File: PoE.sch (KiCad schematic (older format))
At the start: 25 parts, among them IC1 TPS2378DDA

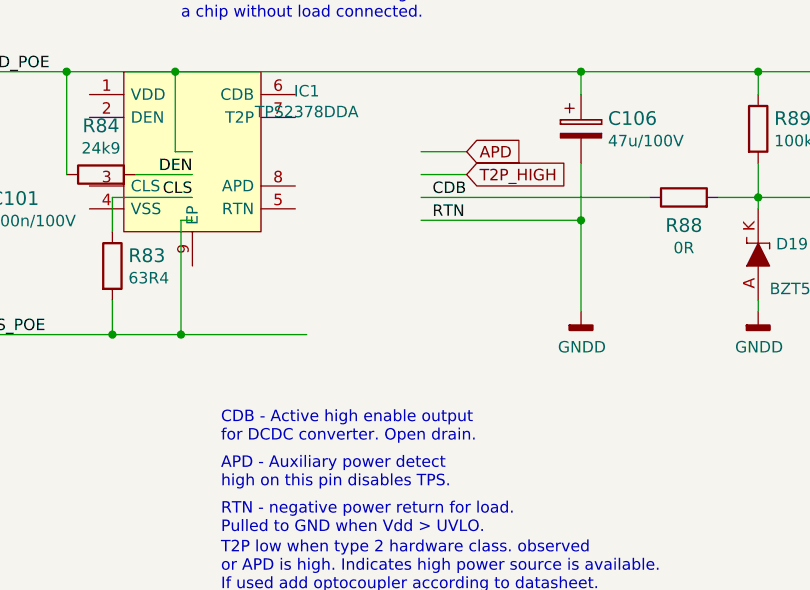
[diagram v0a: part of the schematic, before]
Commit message: Change comment on CDB
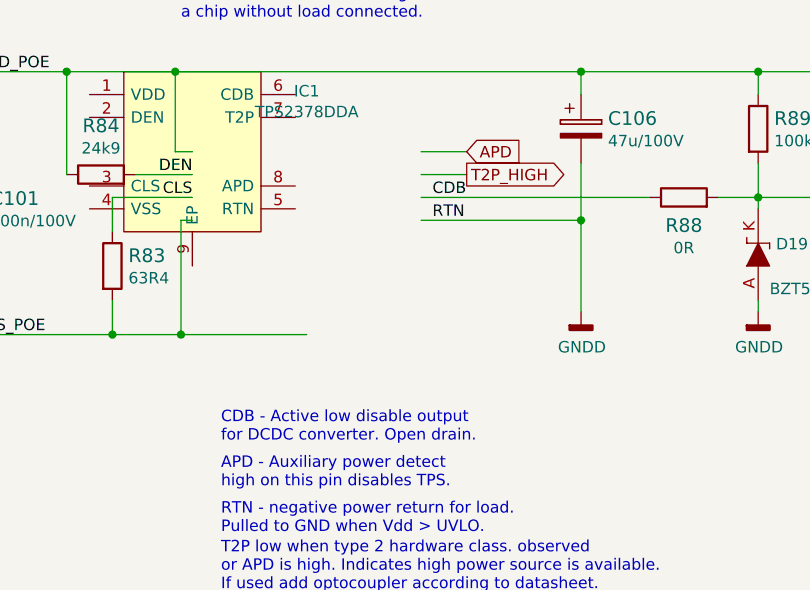
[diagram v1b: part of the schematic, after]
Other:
- note added: "CDB - Active low disable output \nfor DCDC converter. Open drain."
- note removed: "CDB - Active high enable output \nfor DCDC converter. Open drain."
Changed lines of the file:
@@
 $EndComp
 Text Notes 5975 6250 0    50   ~ 0
-CDB - Active high enable output \nfor DCDC converter. Open drain.
+CDB - Active low disable output \nfor DCDC converter. Open drain.
 Wire Wire Line
 	8325 5625 8325 5675
@@
 	1    0    0    -1
 $EndComp
-Text GLabel 7050 5075 2    50   Input ~ 0
+Text GLabel 7050 5075 2    50   Output ~ 0
 T2P_HIGH
 Wire Wire Line

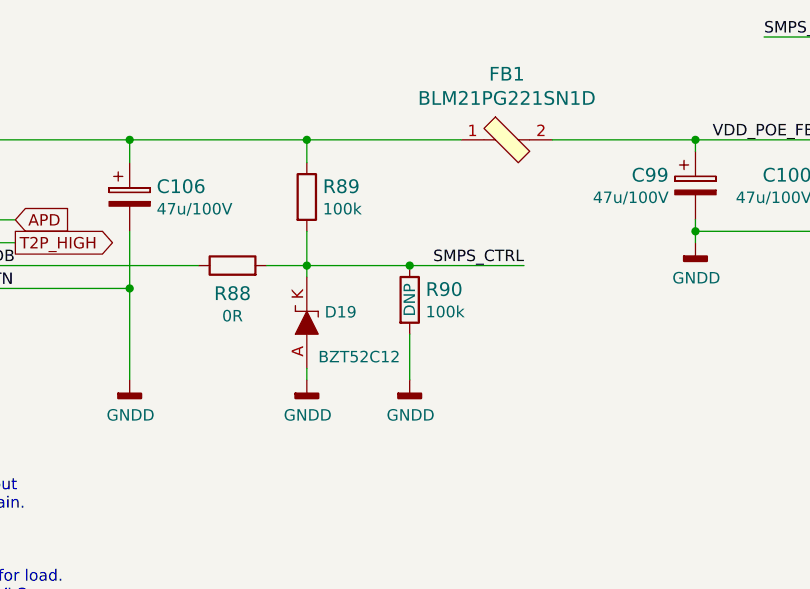
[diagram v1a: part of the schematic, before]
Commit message: Remove zener diode, annotate parts
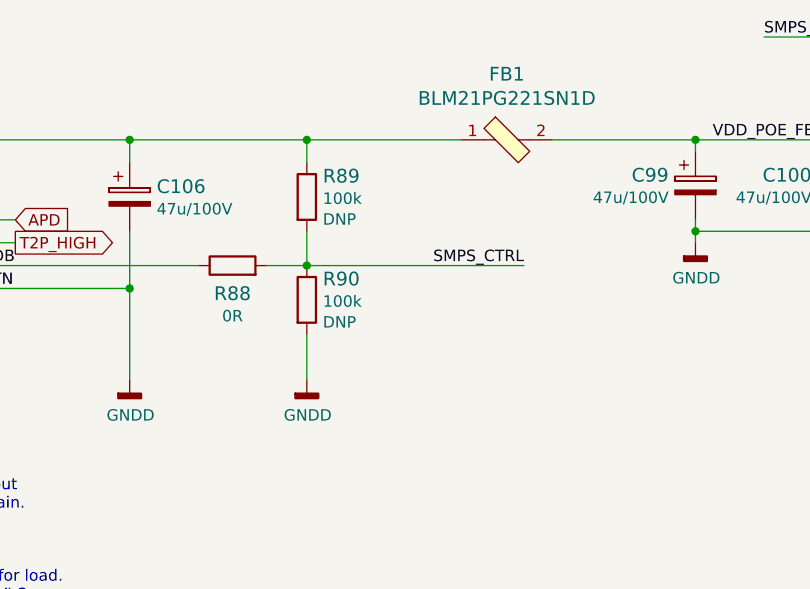
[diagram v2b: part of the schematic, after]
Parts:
- removed D19: BZT52C12, sa800u-baseboard-hw-footprints:SOD-123, symbol sa800u-baseboard-hw:BZT52C12
- R89: DNP (none) -> DNP
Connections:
- wire segments 95 -> 92
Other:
- moved on the sheet: R90
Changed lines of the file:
@@
 Wire Wire Line
 	10875 4825 10775 4825
-Wire Wire Line
-	8775 5175 9275 5175
 Text Label 9275 5175 2    50   ~ 0
 SMPS_CTRL
-Connection ~ 8775 5175
 Wire Wire Line
 	10650 5025 10650 4975
@@
 $EndComp
 Wire Wire Line
-	8775 5475 8775 5675
+	8325 5475 8325 5675
 $Comp
 L sa800u-baseboard-hw:GNDD #PWR0155
 U 1 1 61A460FF
-P 8775 5675
-F 0 "#PWR0155" H 8775 5425 50  0001 C CNN
-F 1 "GNDD" H 8779 5520 50  0000 C CNN
-F 2 "" H 8775 5675 50  0001 C CNN
-F 3 "" H 8775 5675 50  0001 C CNN
-	1    8775 5675
+P 8325 5675
+F 0 "#PWR0155" H 8325 5425 50  0001 C CNN
+F 1 "GNDD" H 8329 5520 50  0000 C CNN
+F 2 "" H 8325 5675 50  0001 C CNN
+F 3 "" H 8325 5675 50  0001 C CNN
+	1    8325 5675
 	1    0    0    -1
 $EndComp
@@
 L sa800u-baseboard-hw:R_100k_0402 R90
 U 1 1 61A46108
-P 8775 5325
-F 0 "R90" V 8730 5395 60  0000 L CNN
-F 1 "R_100k_0402" H 8775 5175 60  0001 C CNN
-F 2 "sa800u-baseboard-hw-footprints:0402-res" H 8975 5525 60  0001 L CNN
-F 3 "" H 8775 5325 50  0001 C CNN
-F 4 "VISHAY" H 8975 5725 60  0001 L CNN "Manufacturer"
-F 5 "CRCW0402100KFKEDHP" H 8975 5625 60  0001 L CNN "MPN"
-F 6 "100k" V 8828 5395 50  0000 L CNN "Val"
-F 7 "DNP" H 8775 5325 50  0000 C CNN "DNP"
-	1    8775 5325
+P 8325 5325
+F 0 "R90" V 8234 5395 60  0000 L CNN
+F 1 "R_100k_0402" H 8325 5175 60  0001 C CNN
+F 2 "sa800u-baseboard-hw-footprints:0402-res" H 8525 5525 60  0001 L CNN
+F 3 "" H 8325 5325 50  0001 C CNN
+F 4 "VISHAY" H 8525 5725 60  0001 L CNN "Manufacturer"
+F 5 "CRCW0402100KFKEDHP" H 8525 5625 60  0001 L CNN "MPN"
+F 6 "100k" V 8332 5395 50  0000 L CNN "Val"
+F 7 "DNP" V 8423 5395 50  0000 L CNN "DNP"
+	1    8325 5325
 	0    1    1    0
 $EndComp
@@
 	1    0    0    -1
 $EndComp
-$Comp
-L sa800u-baseboard-hw:GNDD #PWR0154
-U 1 1 61A46123
-P 8325 5675
-F 0 "#PWR0154" H 8325 5425 50  0001 C CNN
-F 1 "GNDD" H 8329 5520 50  0000 C CNN
-F 2 "" H 8325 5675 50  0001 C CNN
-F 3 "" H 8325 5675 50  0001 C CNN
-	1    8325 5675
-	1    0    0    -1
-$EndComp
 Wire Wire Line
 	8325 5025 8325 5175
@@
 U 1 1 61A46133
 P 8325 4875
-F 0 "R89" V 8280 4945 60  0000 L CNN
+F 0 "R89" V 8234 4945 60  0000 L CNN
 F 1 "R_100k_0402" H 8325 4725 60  0001 C CNN
 F 2 "sa800u-baseboard-hw-footprints:0402-res" H 8525 5075 60  0001 L CNN
@@
 F 4 "VISHAY" H 8525 5275 60  0001 L CNN "Manufacturer"
 F 5 "CRCW0402100KFKEDHP" H 8525 5175 60  0001 L CNN "MPN"
-F 6 "100k" V 8378 4945 50  0000 L CNN "Val"
+F 6 "100k" V 8332 4945 50  0000 L CNN "Val"
+F 7 "DNP" V 8423 4945 50  0000 L CNN "DNP"
 	1    8325 4875
 	0    1    1    0
 $EndComp
-Wire Wire Line
-	8325 5175 8775 5175
 Connection ~ 8325 5175
 Wire Wire Line
@@
 	1    0    0    -1
 $EndComp
-$Comp
-L sa800u-baseboard-hw:BZT52C12 D19
-U 1 1 6286AAC9
-P 8325 5425
-F 0 "D19" V 8371 5347 50  0000 R CNN
-F 1 "BZT52C12" V 8175 5375 50  0000 R CNN
-F 2 "sa800u-baseboard-hw-footprints:SOD-123" H 8325 5425 50  0001 C CNN
-F 3 "https://www.farnell.com/datasheets/1670962.pdf" H 8325 5425 50  0001 C CNN
-F 4 "BZT52C12" H 8325 5425 50  0001 C CNN "MPN"
-F 5 "DIODES INC." H 8325 5425 50  0001 C CNN "Manufacturer"
-	1    8325 5425
-	0    -1   -1   0
-$EndComp
 Text Notes 5975 6250 0    50   ~ 0
 CDB - Active low disable output \nfor DCDC converter. Open drain.
-Wire Wire Line
-	8325 5625 8325 5675
-Wire Wire Line
-	8325 5225 8325 5175
 $Comp
 L sa800u-baseboard-hw:GNDD #PWR0152
@@
 Text Notes 11000 3600 0    79   ~ 16
 5V regulator
+Wire Wire Line
+	8325 5175 9275 5175
 $EndSCHEMATC

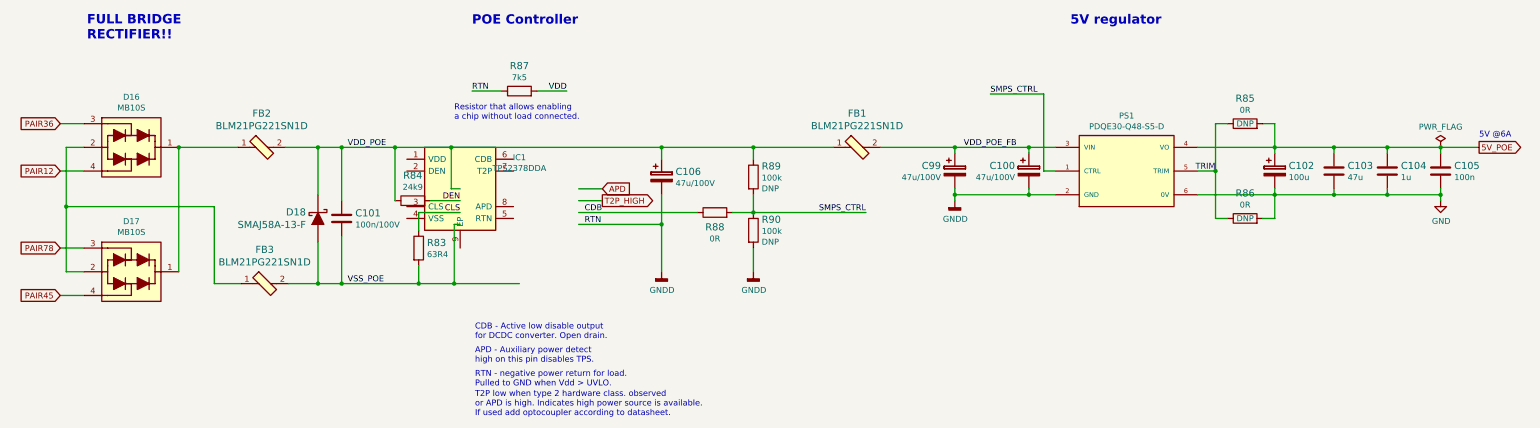
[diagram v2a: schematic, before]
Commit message: Remove ferrite bead and 47uF capacitor
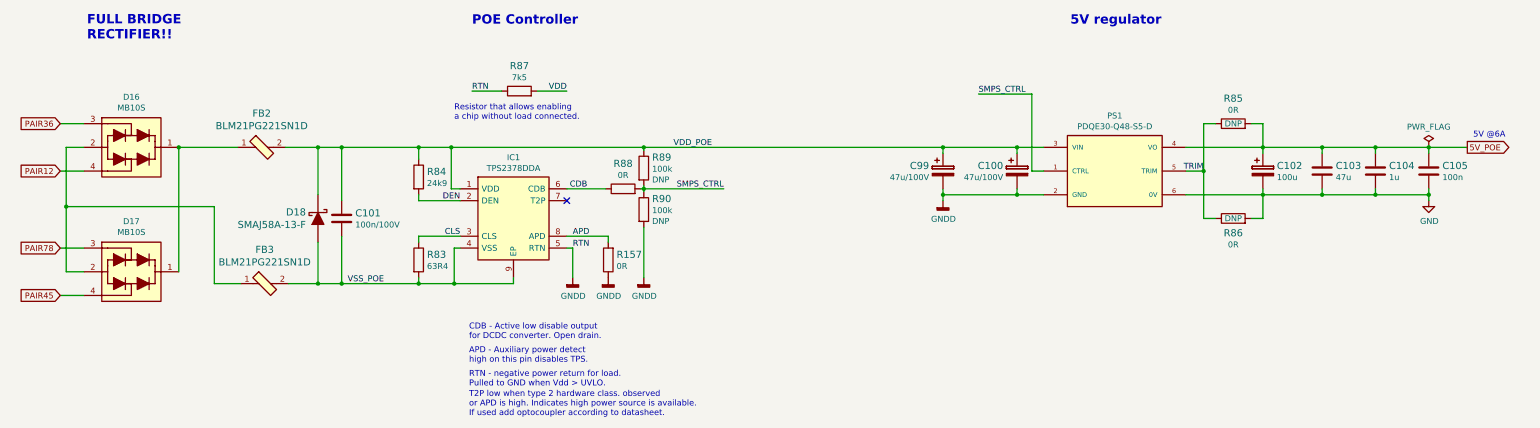
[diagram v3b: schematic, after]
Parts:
- removed C106: C_47u_ELEC_100V, sa800u-baseboard-hw-footprints:CP_Elec_10x10.5, symbol sa800u-baseboard-hw:C_47u_ELEC_100V
- removed FB1: BLM21PG221SN1D, sa800u-baseboard-hw-footprints:0805-res, symbol sa800u-baseboard-hw:BLM21PG221SN1D
- added R157: R_0R_0402, sa800u-baseboard-hw-footprints:0402-res, symbol sa800u-baseboard-hw:R_0R_0402
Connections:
- net labels removed: T2P_HIGH, VDD_POE_FB
- wire segments 92 -> 91
- no-connect marks 0 -> 1
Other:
- moved on the sheet: C100, C102, C103, C104, C105, C99, IC1, PS1, R83, R84, R85, R86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

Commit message: Add additional load to VDD_POE
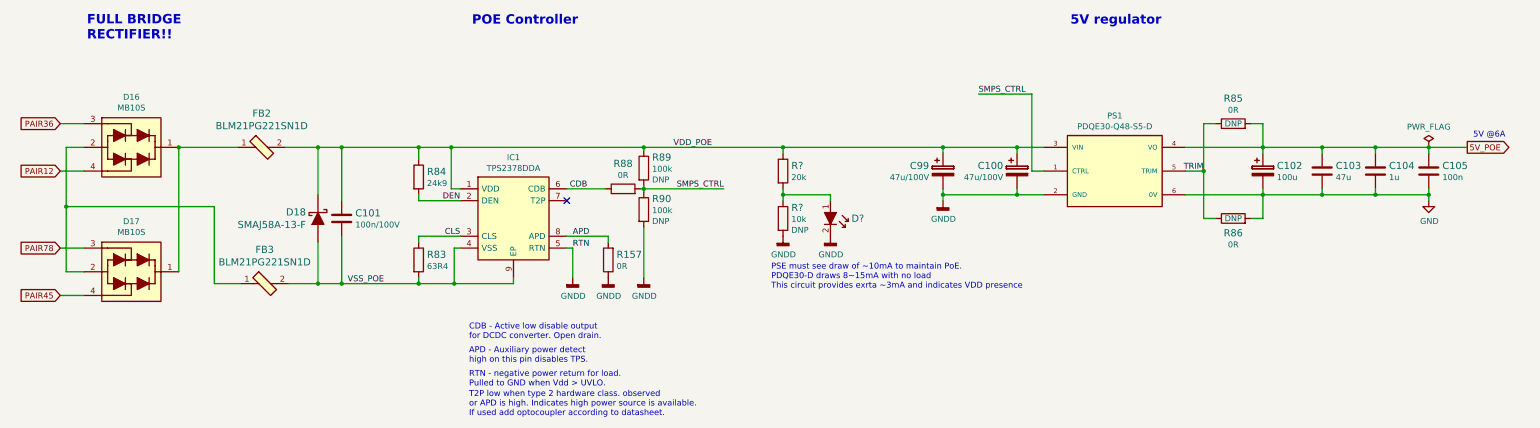
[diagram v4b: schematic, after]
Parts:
- removed R87: R_7k5_0402, sa800u-baseboard-hw-footprints:0402-res, symbol sa800u-baseboard-hw:R_7k5_0402
- added D?: KP-1608EC, sa800u-baseboard-hw-footprints:LED_0603, symbol sa800u-baseboard-hw:KP-1608EC
- added R?: R_20k_0603, sa800u-baseboard-hw-footprints:0603-res, symbol sa800u-baseboard-hw:R_20k_0603
- added R?: R_10k_0603, sa800u-baseboard-hw-footprints:0603-res, symbol sa800u-baseboard-hw:R_10k_0603
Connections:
- net GNDD: now also D?.2, R?.2
- net VDD_POE: now also R?.1
- new net: D?.1, R?.1, R?.2
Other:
- note added: "PSE must see draw of ~~10mA to maintain PoE.\nPDQE30-D draws 8~~15mA with no load\nThis circuit provides exrta ~~3mA and indicates VDD presence"
- note removed: "Resistor that allows enabling\na chip without load connected."
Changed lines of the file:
@@
 	14025 5025 14025 5075
 Wire Wire Line
-	11975 5025 12625 5025
-Wire Wire Line
 	12125 4825 11975 4825
-Text Label 10225 4175 0    50   ~ 0
-SMPS_CTRL
-Wire Wire Line
-	10675 4825 10675 4175
 Wire Wire Line
 	10775 4825 10675 4825
 Text Label 8075 4975 2    50   ~ 0
 SMPS_CTRL
-Wire Wire Line
-	10550 5025 10550 4975
-Wire Wire Line
-	10775 5025 10550 5025
 $Comp
 L sa800u-baseboard-hw:PDQE30-Q48-S5-D PS1
@@
 F 6 "CUI" H 11375 4825 50  0001 L BNN "Manufacturer"
 	1    11375 4825
-	1    0    0    -1
-$EndComp
-$Comp
-L sa800u-baseboard-hw:GNDD #PWR0150
-U 1 1 61A460D6
-P 9925 5075
-F 0 "#PWR0150" H 9925 4825 50  0001 C CNN
-F 1 "GNDD" H 9929 4920 50  0000 C CNN
-F 2 "" H 9925 5075 50  0001 C CNN
-F 3 "" H 9925 5075 50  0001 C CNN
-	1    9925 5075
-	1    0    0    -1
-$EndComp
-$Comp
-L sa800u-baseboard-hw:C_47u_ELEC_100V C100
-U 1 1 61A460E0
-P 10550 4775
-F 0 "C100" H 10433 4770 60  0000 R CNN
-F 1 "C_47u_ELEC_100V" H 10550 4625 60  0001 C CNN
-F 2 "sa800u-baseboard-hw-footprints:CP_Elec_10x10.5" H 10750 4975 60  0001 L CNN
-F 3 "https://industrial.panasonic.com/cdbs/www-data/pdf/RDE0000/ABA0000C1151.pdf" H 10550 4775 50  0001 C CNN
-F 4 "PANASONIC" H 10750 5175 60  0001 L CNN "Manufacturer"
-F 5 "EEEHA2A470UP" H 10750 5075 60  0001 L CNN "MPN"
-F 6 "47u/100V" H 10433 4672 50  0000 R CNN "Val"
-	1    10550 4775
-	1    0    0    -1
-$EndComp
-$Comp
-L sa800u-baseboard-hw:C_47u_ELEC_100V C99
-U 1 1 61A460EB
-P 9925 4775
-F 0 "C99" H 9808 4770 60  0000 R CNN
-F 1 "C_47u_ELEC_100V" H 9925 4625 60  0001 C CNN
-F 2 "sa800u-baseboard-hw-footprints:CP_Elec_10x10.5" H 10125 4975 60  0001 L CNN
-F 3 "https://industrial.panasonic.com/cdbs/www-data/pdf/RDE0000/ABA0000C1151.pdf" H 9925 4775 50  0001 C CNN
-F 4 "PANASONIC" H 10125 5175 60  0001 L CNN "Manufacturer"
-F 5 "EEEHA2A470UP" H 10125 5075 60  0001 L CNN "MPN"
-F 6 "47u/100V" H 9808 4672 50  0000 R CNN "Val"
-	1    9925 4775
 	1    0    0    -1
 $EndComp
@@
 Text Notes 5925 6900 0    50   ~ 0
 T2P low when type 2 hardware class. observed\nor APD is high. Indicates high power source is available. \nIf used add optocoupler according to datasheet.
-Text Notes 5800 4400 0    50   ~ 0
-Resistor that allows enabling\na chip without load connected.
 Text Label 6800 5475 0    50   ~ 0
 RTN
@@
 Connection ~ 13575 5025
 Connection ~ 13125 5025
-Wire Wire Line
-	10550 4625 10550 4675
-Wire Wire Line
-	9925 4975 9925 5025
-Wire Wire Line
-	9925 4625 9925 4675
 Connection ~ 10550 4625
 Wire Wire Line
 	10550 4625 10775 4625
-Connection ~ 10550 5025
-Connection ~ 9925 4625
 Wire Wire Line
 	9925 4625 10550 4625
-Connection ~ 9925 5025
-Wire Wire Line
-	9925 5025 10550 5025
-Wire Wire Line
-	9925 5075 9925 5025
 Connection ~ 4650 4625
 Connection ~ 4650 5775
@@
 Text Label 6775 4975 0    50   ~ 0
 CDB
-Text Label 5950 4150 0    50   ~ 0
-RTN
-Wire Wire Line
-	6200 4150 5950 4150
-Wire Wire Line
-	6750 4150 6500 4150
-Text Label 6750 4150 2    50   ~ 0
-VDD
 $Comp
 L sa800u-baseboard-hw:TPS2378DDA IC1
@@
 Text Label 7650 4625 0    50   ~ 0
 VDD_POE
-$Comp
-L sa800u-baseboard-hw:R_7k5_0402 R87
-U 1 1 66578F6C
-P 6350 4150
-F 0 "R87" H 6350 4363 60  0000 C CNN
-F 1 "R_7k5_0402" H 6350 4000 60  0001 C CNN
-F 2 "sa800u-baseboard-hw-footprints:0402-res" H 6550 4350 60  0001 L CNN
-F 3 "" H 6350 4150 50  0001 C CNN
-F 4 "YAGEO" H 6550 4550 60  0001 L CNN "Manufacturer"
-F 5 "RC0402FR-077K5L" H 6550 4450 60  0001 L CNN "MPN"
-F 6 "7k5" H 6350 4265 50  0000 C CNN "Val"
-	1    6350 4150
-	1    0    0    -1
-$EndComp
 Text Label 5850 5075 2    50   ~ 0
 DEN
@@
 	12525 4425 12625 4425
 Wire Wire Line
-	10225 4175 10675 4175
-Wire Wire Line
 	12125 4425 12225 4425
 Wire Wire Line
@@
 Wire Wire Line
 	7400 4650 7400 4625
-Connection ~ 7400 4625
 Wire Wire Line
 	5775 4625 7400 4625
@@
 Text GLabel 2475 5475 0    50   Input ~ 0
 PAIR78
-Wire Wire Line
-	7400 4625 9925 4625
+Connection ~ 9925 4625
+Connection ~ 7400 4625
+Wire Wire Line
+	7400 4625 8575 4625
+$Comp
+L sa800u-baseboard-hw:GNDD #PWR0150
+U 1 1 61A460D6
+P 9925 5075
+F 0 "#PWR0150" H 9925 4825 50  0001 C CNN
+F 1 "GNDD" H 9929 4920 50  0000 C CNN
+F 2 "" H 9925 5075 50  0001 C CNN
+F 3 "" H 9925 5075 50  0001 C CNN
+	1    9925 5075
+	1    0    0    -1
+$EndComp
+Wire Wire Line
+	9925 5075 9925 5025
+Connection ~ 9925 5025
+Wire Wire Line
+	9925 5025 10550 5025
+Wire Wire Line
+	10550 5025 10550 4975
+Wire Wire Line
+	10550 4625 10550 4675
+$Comp
+L sa800u-baseboard-hw:C_47u_ELEC_100V C100
+U 1 1 61A460E0
+P 10550 4775
+F 0 "C100" H 10433 4770 60  0000 R CNN
+F 1 "C_47u_ELEC_100V" H 10550 4625 60  0001 C CNN
+F 2 "sa800u-baseboard-hw-footprints:CP_Elec_10x10.5" H 10750 4975 60  0001 L CNN
+F 3 "https://industrial.panasonic.com/cdbs/www-data/pdf/RDE0000/ABA0000C1151.pdf" H 10550 4775 50  0001 C CNN
+F 4 "PANASONIC" H 10750 5175 60  0001 L CNN "Manufacturer"
+F 5 "EEEHA2A470UP" H 10750 5075 60  0001 L CNN "MPN"
+F 6 "47u/100V" H 10433 4672 50  0000 R CNN "Val"
+	1    10550 4775
+	1    0    0    -1
+$EndComp
+Wire Wire Line
+	9925 4975 9925 5025
+Wire Wire Line
+	9925 4625 9925 4675
+$Comp
+L sa800u-baseboard-hw:C_47u_ELEC_100V C99
+U 1 1 61A460EB
+P 9925 4775
+F 0 "C99" H 9808 4770 60  0000 R CNN
+F 1 "C_47u_ELEC_100V" H 9925 4625 60  0001 C CNN
+F 2 "sa800u-baseboard-hw-footprints:CP_Elec_10x10.5" H 10125 4975 60  0001 L CNN
+F 3 "https://industrial.panasonic.com/cdbs/www-data/pdf/RDE0000/ABA0000C1151.pdf" H 9925 4775 50  0001 C CNN
+F 4 "PANASONIC" H 10125 5175 60  0001 L CNN "Manufacturer"
+F 5 "EEEHA2A470UP" H 10125 5075 60  0001 L CNN "MPN"
+F 6 "47u/100V" H 9808 4672 50  0000 R CNN "Val"
+	1    9925 4775
+	1    0    0    -1
+$EndComp
+Wire Wire Line
+	10225 4175 10675 4175
+Wire Wire Line
+	10675 4825 10675 4175
+Text Label 10225 4175 0    50   ~ 0
+SMPS_CTRL
+Connection ~ 10550 5025
+Wire Wire Line
+	10775 5025 10550 5025
+Wire Wire Line
+	11975 5025 12625 5025
+$Comp
+L sa800u-baseboard-hw:R_20k_0603 R?
+U 1 1 62C10670
+P 8575 4825
+F 0 "R?" V 8530 4895 60  0000 L CNN
+F 1 "R_20k_0603" H 8575 4675 60  0001 C CNN
+F 2 "sa800u-baseboard-hw-footprints:0603-res" H 8775 5025 60  0001 L CNN
+F 3 "" H 8575 4825 50  0001 C CNN
+F 4 "MULTICOMP" H 8775 5225 60  0001 L CNN "Manufacturer"
+F 5 "MCMR06X203_JTL" H 8775 5125 60  0001 L CNN "MPN"
+F 6 "20k" V 8628 4895 50  0000 L CNN "Val"
+	1    8575 4825
+	0    1    1    0
+$EndComp
+Wire Wire Line
+	8575 4625 8575 4675
+Wire Wire Line
+	8575 4975 8575 5025
+$Comp
+L sa800u-baseboard-hw:R_10k_0603 R?
+U 1 1 62C1B70F
+P 8575 5225
+F 0 "R?" V 8484 5295 60  0000 L CNN
+F 1 "R_10k_0603" H 8575 5075 60  0001 C CNN
+F 2 "sa800u-baseboard-hw-footprints:0603-res" H 8775 5425 60  0001 L CNN
+F 3 "" H 8575 5225 50  0001 C CNN
+F 4 "BOURNS" H 8775 5625 60  0001 L CNN "Manufacturer"
+F 5 "CR0603-JW-103ELF" H 8775 5525 60  0001 L CNN "MPN"
+F 6 "10k" V 8582 5295 50  0000 L CNN "Val"
+F 7 "DNP" V 8673 5295 50  0000 L CNN "DNP"
+	1    8575 5225
+	0    1    1    0
+$EndComp
+$Comp
+L sa800u-baseboard-hw:GNDD #PWR?
+U 1 1 62C1C906
+P 8575 5375
+F 0 "#PWR?" H 8575 5125 50  0001 C CNN
+F 1 "GNDD" H 8579 5220 50  0000 C CNN
+F 2 "" H 8575 5375 50  0001 C CNN
+F 3 "" H 8575 5375 50  0001 C CNN
+	1    8575 5375
+	1    0    0    -1
+$EndComp
+Wire Wire Line
+	8575 5025 8975 5025
+Wire Wire Line
+	8975 5025 8975 5075
+Connection ~ 8575 5025
+Wire Wire Line
+	8575 5025 8575 5075
+$Comp
+L sa800u-baseboard-hw:KP-1608EC D?
+U 1 1 62C25BE8
+P 8975 5275
+F 0 "D?" V 8925 5453 60  0000 L CNN
+F 1 "KP-1608EC" V 8978 5453 60  0001 L CNN
+F 2 "sa800u-baseboard-hw-footprints:LED_0603" H 9175 5475 60  0001 L CNN
+F 3 "https://www.farnell.com/datasheets/1854072.pdf" H 9175 5575 60  0001 L CNN
+F 4 "KP-1608EC" H 9175 5775 60  0001 L CNN "MPN"
+F 5 "KINGBRIGHT" H 9185 5895 60  0001 L CNN "Manufacturer"
+	1    8975 5275
+	0    1    1    0
+$EndComp
+$Comp
+L sa800u-baseboard-hw:GNDD #PWR?
+U 1 1 62C271AD
+P 8975 5375
+F 0 "#PWR?" H 8975 5125 50  0001 C CNN
+F 1 "GNDD" H 8979 5220 50  0000 C CNN
+F 2 "" H 8975 5375 50  0001 C CNN
+F 3 "" H 8975 5375 50  0001 C CNN
+	1    8975 5375
+	1    0    0    -1
+$EndComp
+Connection ~ 8575 4625
+Wire Wire Line
+	8575 4625 9925 4625
+Text Notes 8475 5825 0    50   ~ 0
+PSE must see draw of ~~10mA to maintain PoE.\nPDQE30-D draws 8~~15mA with no load\nThis circuit provides exrta ~~3mA and indicates VDD presence
 $EndSCHEMATC
